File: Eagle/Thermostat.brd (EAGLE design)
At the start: 67.1 x 49.3 mm, 56 parts, among them J2 USB-MINIB-5PIN, K1 AQY282EHA, K2 AQY282EHA, K3 AQY282EHA, K4 AQY282EHA, K5 AQY282EHA, Q1 MOSFET-PCHANNELSMD

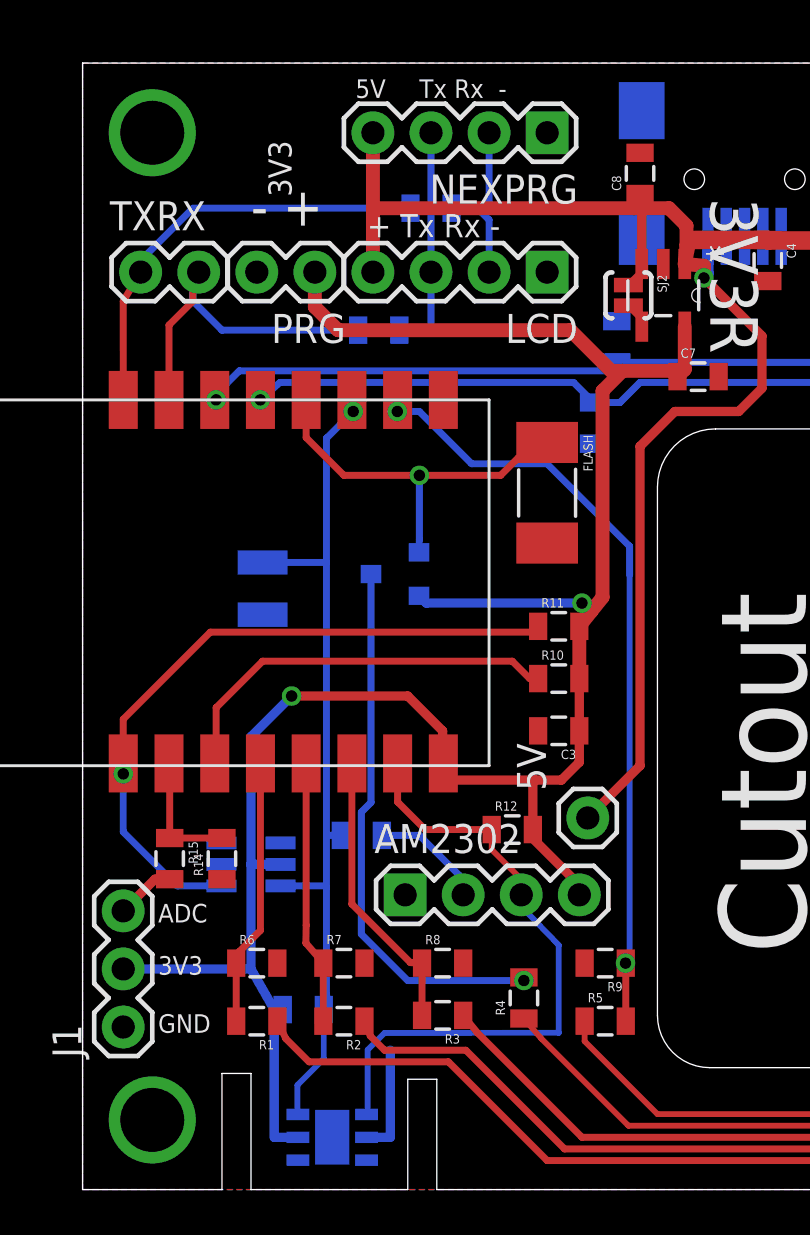
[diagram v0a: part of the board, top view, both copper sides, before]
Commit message: Added R19 (optional)
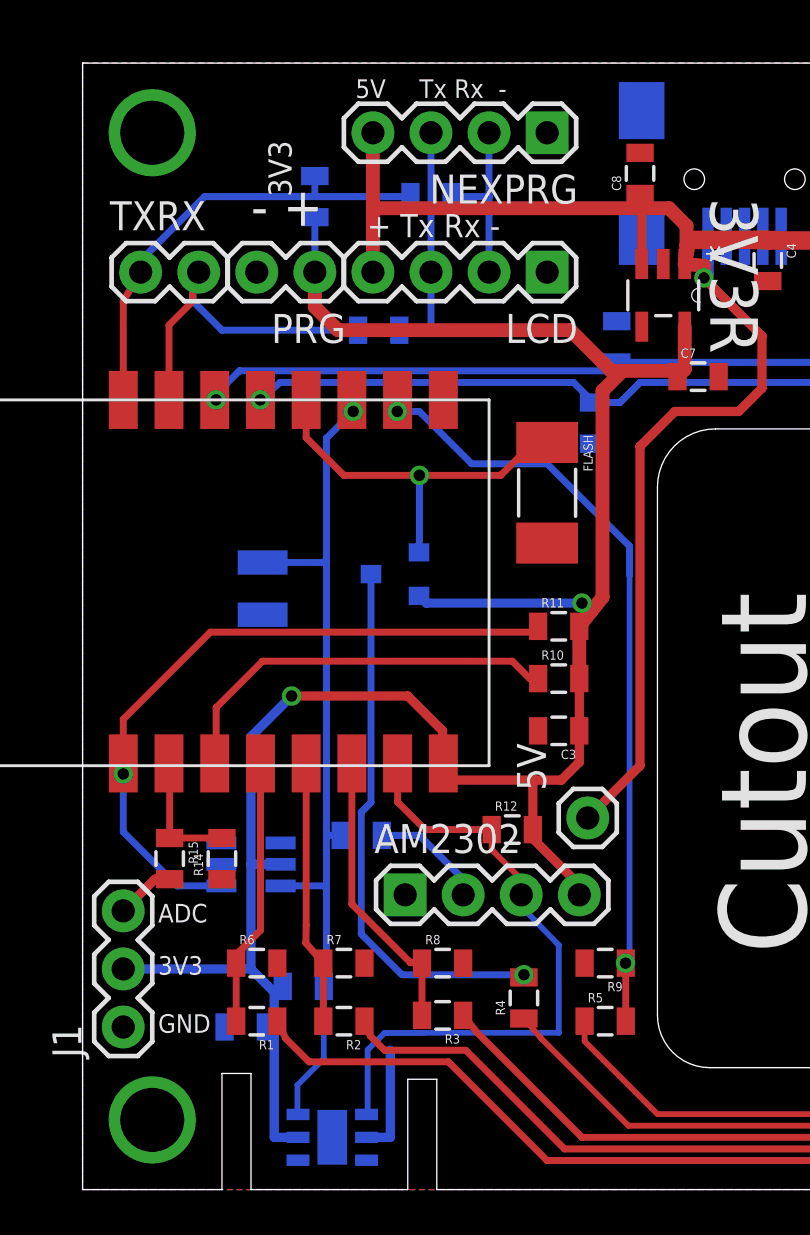
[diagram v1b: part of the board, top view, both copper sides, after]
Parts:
- removed SJ2: MCP1804-OPT, SparkFun-Retired:SJ_2S-NO
- added C9: 0.1uF, SparkFun-Capacitors:0805
- added R19: 10K, SparkFun-Resistors:0805
- R12, R13: value 10K -> 4K7
- R16: value 5K6 -> 1K
- moved R13 1.02 mm to (9.65, 8.89)
- moved R17 0.51 mm to (15.2, 43.4)
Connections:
- removed net N$1: 3V3R.4, SJ2.2
- net 3V3: now also C9.1, R19.1
- net 5V: no longer SJ2.1
- net GND: now also C9.2
- net TXD: now also R19.2
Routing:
- net 3V3: track 97.9 -> 100.9 mm
- net SCL: track 38.0 -> 39.2 mm
- net N$1: track 1.16 -> 0.00 mm
- net TXD: track 19.1 -> 20.2 mm
- net 5V: track 92.5 -> 91.7 mm
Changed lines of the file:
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@@
 <attribute name="OC_FARNELL" value="1578370" x="25.4" y="39.116" size="1.4224" layer="27" ratio="16" rot="R270" display="off"/>
 </element>
-<element name="R17" library="SparkFun-Resistors" package="0805" value="5K6" x="15.24" y="42.926" rot="MR180"/>
+<element name="R17" library="SparkFun-Resistors" package="0805" value="5K6" x="15.24" y="43.434" rot="MR180"/>
 <element name="10F" library="Microchip_By_element14_Batch_1" package="SOT95P270X145-6N" value="PIC10F202T-I/OT" x="7.366" y="14.224" rot="MR180">
 <attribute name="OC_FARNELL" value="9942874" x="7.366" y="14.224" size="0.8128" layer="28" ratio="16" rot="MR180" display="off"/>
@@
 </element>
 <element name="Q1" library="SparkFun-DiscreteSemi" package="SOT23-3" value="MOSFET-PCHANNELSMD" x="13.716" y="26.924" rot="MR270"/>
-<element name="R12" library="SparkFun-Resistors" package="0805" value="10K" x="18.796" y="15.748"/>
-<element name="R13" library="SparkFun-Resistors" package="0805" value="10K" x="9.652" y="7.874" rot="MR0"/>
+<element name="R12" library="SparkFun-Resistors" package="0805" value="4K7" x="18.796" y="15.748"/>
+<element name="R13" library="SparkFun-Resistors" package="0805" value="4K7" x="9.652" y="8.89" rot="MR0"/>
 <element name="NEXPRG" library="SparkFun-Connectors" package="1X04" value="" x="20.32" y="46.228" rot="R180"/>
 <element name="U$2" library="CuriousTech" package="SMD-PAD1" value="SMD-PAD1" x="7.874" y="25.146" rot="MR0"/>
 <element name="U$5" library="CuriousTech" package="SMD-PAD1" value="SMD-PAD1" x="7.874" y="27.432" rot="MR0"/>
-<element name="R16" library="SparkFun-Resistors" package="0805" value="5K6" x="12.954" y="37.592" rot="MR180"/>
+<element name="R16" library="SparkFun-Resistors" package="0805" value="1K" x="12.954" y="37.592" rot="MR180"/>
 <element name="J1" library="SparkFun-Connectors" package="1X03" value="" x="1.778" y="7.112" rot="R90"/>
 <element name="J2" library="SparkFun-Connectors" package="USB-MINIB" value="USB-MINIB-5PIN" x="28.956" y="44.196" rot="MR270">
 <attribute name="PROD_ID" value="CONN-08193" x="28.956" y="44.196" size="1.4224" layer="28" ratio="16" rot="MR270" display="off"/>
 </element>
-<element name="SJ2" library="SparkFun-Retired" package="SJ_2S-NO" value="MCP1804-OPT" x="23.876" y="39.116" rot="R270"/>
 <element name="5VSWPP" library="CuriousTech" package="SO08" value="MIC4680" x="56.642" y="44.958" rot="R270"/>
 <element name="C8" library="SparkFun-Capacitors" package="0805" value="1uF" x="24.384" y="44.45" rot="R90"/>
@@
 <element name="5V" library="SparkFun-Connectors" package="1X01" value="" x="22.098" y="16.256" rot="R90"/>
 <element name="SHT21" library="CuriousTech" package="SHT21" value="SHT-21" x="10.922" y="2.286" rot="MR0"/>
+<element name="C9" library="SparkFun-Capacitors" package="0805" value="0.1uF" x="7.112" y="7.112" rot="MR0"/>
+<element name="R19" library="SparkFun-Resistors" package="0805" value="10K" x="10.16" y="43.434" rot="MR90"/>
 </elements>
 <signals>
@@
 <wire x1="12.422" y1="2.286" x2="13.462" y2="2.286" width="0.4064" layer="16"/>
 <wire x1="13.462" y1="2.286" x2="13.462" y2="6.096" width="0.4064" layer="16"/>
+<contactref element="C9" pad="2"/>
 </signal>
 <signal name="N$24">
@@
 <wire x1="23.622" y1="35.814" x2="25.77" y2="35.814" width="0.6096" layer="1"/>
 <wire x1="25.77" y1="35.814" x2="26.024" y2="35.56" width="0.6096" layer="1"/>
-<wire x1="8.382" y1="2.286" x2="8.382" y2="7.874" width="0.4064" layer="16"/>
-<wire x1="8.382" y1="7.874" x2="7.366" y2="9.652" width="0.4064" layer="16"/>
-<wire x1="8.752" y1="7.874" x2="8.382" y2="7.874" width="0.4064" layer="16"/>
+<wire x1="8.382" y1="2.286" x2="8.382" y2="7.112" width="0.4064" layer="16"/>
+<wire x1="8.382" y1="7.112" x2="8.382" y2="8.636" width="0.4064" layer="16"/>
+<wire x1="8.382" y1="8.636" x2="7.366" y2="9.652" width="0.4064" layer="16"/>
+<wire x1="8.752" y1="8.89" x2="8.382" y2="8.636" width="0.4064" layer="16"/>
 <wire x1="22.744" y1="34.936" x2="23.622" y2="35.814" width="0.6096" layer="1"/>
 <wire x1="19.696" y1="15.748" x2="19.696" y2="15.356" width="0.4064" layer="1"/>
@@
 <wire x1="14.716" y1="25.974" x2="15.036" y2="25.654" width="0.4064" layer="16"/>
 <wire x1="15.036" y1="25.654" x2="21.844" y2="25.654" width="0.4064" layer="16"/>
+<contactref element="C9" pad="1"/>
+<wire x1="8.012" y1="7.112" x2="8.382" y2="7.112" width="0.254" layer="16"/>
+<contactref element="R19" pad="1"/>
+<wire x1="10.16" y1="42.534" x2="10.16" y2="40.132" width="0.3048" layer="16"/>
 </signal>
 <signal name="TXD">
@@
 <wire x1="1.778" y1="38.862" x2="1.78" y2="34.542" width="0.3048" layer="1"/>
 <wire x1="2.54" y1="40.132" x2="2.54" y2="40.64" width="0.3048" layer="16"/>
-<wire x1="2.54" y1="40.64" x2="4.826" y2="42.926" width="0.3048" layer="16"/>
+<wire x1="2.54" y1="40.64" x2="5.334" y2="43.434" width="0.3048" layer="16"/>
 <contactref element="R17" pad="1"/>
-<wire x1="14.34" y1="42.926" x2="4.826" y2="42.926" width="0.3048" layer="16"/>
+<wire x1="14.34" y1="43.434" x2="10.16" y2="43.434" width="0.3048" layer="16"/>
+<contactref element="R19" pad="2"/>
+<wire x1="10.16" y1="43.434" x2="5.334" y2="43.434" width="0.3048" layer="16"/>
+<wire x1="10.16" y1="44.334" x2="10.16" y2="43.434" width="0.3048" layer="16"/>
 </signal>
 <signal name="RXD">
@@
 <wire x1="27.178" y1="39.878" x2="27.178" y2="40.4114" width="0.6096" layer="1"/>
 <wire x1="27.178" y1="40.4114" x2="26.3398" y2="40.4876" width="0.6096" layer="1"/>
-<contactref element="SJ2" pad="1"/>
 <wire x1="24.4602" y1="40.4876" x2="24.4602" y2="40.1502" width="0.3048" layer="1"/>
-<wire x1="24.4602" y1="40.1502" x2="23.876" y2="39.566" width="0.3048" layer="1"/>
 <contactref element="5VSWPP" pad="4"/>
 <wire x1="54.042" y1="43.053" x2="51.059" y2="43.053" width="0.8128" layer="1"/>
@@
 <wire x1="10.668" y1="15.494" x2="10.668" y2="13.208" width="0.3048" layer="16"/>
 <wire x1="10.668" y1="13.208" x2="10.668" y2="8.5344" width="0.3048" layer="16"/>
-<wire x1="10.668" y1="8.5344" x2="10.7442" y2="8.2042" width="0.3048" layer="16"/>
+<wire x1="10.668" y1="8.5344" x2="10.4902" y2="8.7122" width="0.3048" layer="16"/>
 <contactref element="10F" pad="6"/>
 <wire x1="8.6614" y1="13.2842" x2="10.5918" y2="13.2842" width="0.3048" layer="16"/>
@@
 <contactref element="U$5" pad="&gt;NAME"/>
 <wire x1="7.874" y1="27.432" x2="10.668" y2="27.432" width="0.3048" layer="16"/>
-<wire x1="10.552" y1="7.874" x2="10.7442" y2="7.874" width="0.3048" layer="16"/>
-<wire x1="10.7442" y1="7.874" x2="10.7442" y2="8.2042" width="0.3048" layer="16"/>
+<wire x1="10.552" y1="8.89" x2="10.4902" y2="8.382" width="0.3048" layer="16"/>
+<wire x1="10.4902" y1="8.382" x2="10.4902" y2="8.7122" width="0.3048" layer="16"/>
 <contactref element="R18" pad="1"/>
 <wire x1="11.292" y1="15.494" x2="10.668" y2="15.494" width="0.3048" layer="16"/>
@@
 <wire x1="9.398" y1="3.3098" x2="9.398" y2="4.572" width="0.254" layer="16"/>
 <wire x1="9.398" y1="4.572" x2="10.552" y2="5.726" width="0.254" layer="16"/>
-<wire x1="10.552" y1="7.874" x2="10.552" y2="5.726" width="0.254" layer="16"/>
+<wire x1="10.552" y1="8.89" x2="10.552" y2="5.726" width="0.254" layer="16"/>
 </signal>
 <signal name="SDA">
@@
 <contactref element="R17" pad="2"/>
 <contactref element="LCD" pad="2"/>
-<wire x1="16.14" y1="42.926" x2="17.272" y2="42.926" width="0.3048" layer="16"/>
-<wire x1="17.78" y1="42.418" x2="17.78" y2="40.132" width="0.3048" layer="16"/>
-<wire x1="17.272" y1="42.926" x2="17.399" y2="42.799" width="0.3048" layer="16"/>
+<wire x1="16.14" y1="43.434" x2="17.78" y2="43.434" width="0.3048" layer="16"/>
+<wire x1="17.78" y1="43.434" x2="17.78" y2="40.132" width="0.3048" layer="16"/>
 <contactref element="NEXPRG" pad="2"/>
-<wire x1="17.399" y1="42.799" x2="17.78" y2="42.418" width="0.3048" layer="16"/>
-<wire x1="17.78" y1="46.228" x2="17.78" y2="43.18" width="0.3048" layer="16"/>
-<wire x1="17.78" y1="43.18" x2="17.399" y2="42.799" width="0.3048" layer="16"/>
+<wire x1="17.78" y1="46.228" x2="17.78" y2="43.434" width="0.3048" layer="16"/>
 </signal>
 <signal name="REST">
@@
 <wire x1="12.616" y1="16.934" x2="12.192" y2="16.51" width="0.3048" layer="16"/>
 <wire x1="12.192" y1="16.51" x2="12.192" y2="11.176" width="0.3048" layer="16"/>
-<wire x1="12.192" y1="11.176" x2="14.224" y2="9.144" width="0.3048" layer="16"/>
-<wire x1="14.224" y1="9.144" x2="19.304" y2="9.144" width="0.3048" layer="16"/>
-<via x="19.304" y="9.144" extent="1-16" drill="0.5" shape="square"/>
-<wire x1="19.304" y1="9.144" x2="19.696" y2="9.144" width="0.3048" layer="1"/>
+<wire x1="19.304" y1="9.3" x2="19.696" y2="9.144" width="0.3048" layer="1"/>
 <wire x1="19.696" y1="9.144" x2="19.304" y2="9.282" width="0.3048" layer="1"/>
+<wire x1="12.192" y1="11.176" x2="13.97" y2="9.398" width="0.3048" layer="16"/>
+<wire x1="13.97" y1="9.398" x2="19.304" y2="9.398" width="0.3048" layer="16"/>
+<via x="19.304" y="9.398" extent="1-16" drill="0.5" shape="square"/>
+<wire x1="19.304" y1="9.398" x2="19.188" y2="9.398" width="0.3048" layer="1"/>
+<wire x1="19.188" y1="9.398" x2="19.304" y2="9.282" width="0.3048" layer="1"/>
 </signal>
 <signal name="HUMID">
@@
 <wire x1="15.24" y1="46.228" x2="15.24" y2="40.132" width="0.3048" layer="16"/>
 </signal>
-<signal name="N$1">
-<contactref element="3V3R" pad="4"/>
-<contactref element="SJ2" pad="2"/>
-<wire x1="24.4602" y1="37.7444" x2="24.4602" y2="38.0818" width="0.3048" layer="1"/>
-<wire x1="24.4602" y1="38.0818" x2="23.876" y2="38.666" width="0.3048" layer="1"/>
-</signal>
 <signal name="N$16">
